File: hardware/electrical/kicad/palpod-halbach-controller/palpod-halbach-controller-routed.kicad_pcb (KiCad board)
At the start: 4 copper layers, 150 x 100 mm, 60 parts, among them Q1 IPI050N06N, Q10 IPI050N06N, Q11 IPI050N06N, Q12 IPI050N06N, Q2 IPI050N06N, Q3 IPI050N06N, Q4 IPI050N06N, Q5 IPI050N06N, Q6 IPI050N06N, Q7 IPI050N06N, Q8 IPI050N06N, Q9 IPI050N06N, U1 STM32H723ZGT6 (Primary), U10 MLX90393 #4, U11 MLX90393 #5, U12 MLX90393 #6, U13 DRV8323 CH1, U14 DRV8323 CH2, U15 DRV8323 CH3, U16 DRV8323 CH4, U17 DRV8323 CH5, U18 DRV8323 CH6, U2 STM32H723ZGT6 (Redundant), U25 INA240, U26 INA240, U27 INA240, U28 INA240, U29 INA240, U3 MAX706, U30 INA240, U4 TL331, U5 MCP2542FD, U6 STM32G030K8T6, U7 MLX90393 #1, U8 MLX90393 #2, U9 MLX90393 #3

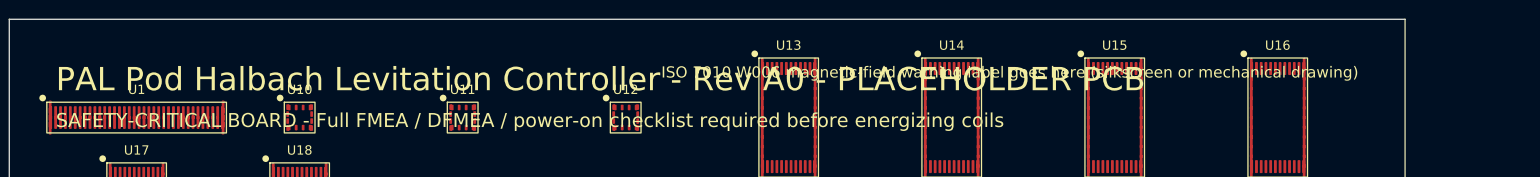
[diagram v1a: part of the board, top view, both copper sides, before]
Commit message: brand: broad KiCad sweep — remaining PAL Pod strings → Hearth
Targeted-pattern sed in ff14a48 missed variants. Broad find-replace
on .kicad_sch/pcb/pro/sym/mod + fp-lib-table + sym-lib-table +
per-project README.md (only where PAL Pod string actually appeared).
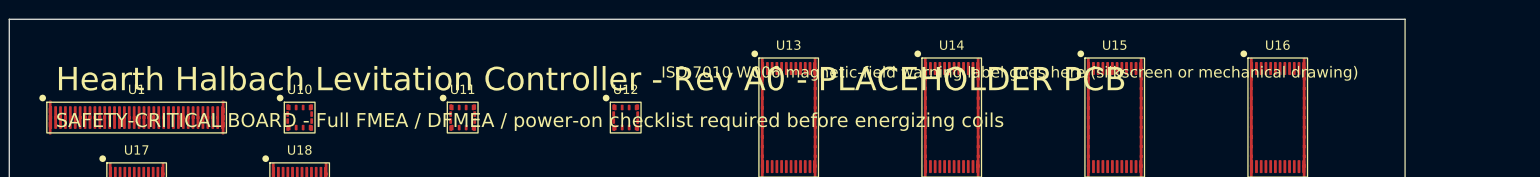
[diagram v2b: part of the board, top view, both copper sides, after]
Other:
- board text added: "Hearth Halbach Levitation Controller - Rev A0 - PLACEHOLDER PCB"
- board text removed: "PAL Pod Halbach Levitation Controller - Rev A0 - PLACEHOLDER PCB"
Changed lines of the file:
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@@
 	(paper "A3")
 	(title_block
-		(title "PAL Pod Halbach Levitation Controller - PCB")
+		(title "Hearth Halbach Levitation Controller - PCB")
 		(date "2026-08-03")
 		(rev "A0")
@@
 		)
 	)
-	(gr_text "PAL Pod Halbach Levitation Controller - Rev A0 - PLACEHOLDER PCB"
+	(gr_text "Hearth Halbach Levitation Controller - Rev A0 - PLACEHOLDER PCB"
 		(at 55 55 0)
 		(layer "F.SilkS")
